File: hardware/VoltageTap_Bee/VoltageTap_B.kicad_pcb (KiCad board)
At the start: 2 copper layers, 50 x 105 mm, 144 parts, among them J1 Conn_01x09_Socket, J101 HRLV, J102 Conn_01x18_Pin, J16 USB_B_Micro, Q6 2N7002, U10 MCP2542FDxMF, U12 FT230XS, U2 MCU-MSM0G3507SPM, U203 2PD2150-QX, U204 2PD2150-QX, U205 2PD2150-QX, U206 2PD2150-QX, U207 2PD2150-QX, U208 2PD2150-QX, U209 2PD2150-QX, U210 2PD2150-QX, U211 2PD2150-QX, U212 2PD2150-QX, U213 2PD2150-QX, U214 2PD2150-QX, U215 2PD2150-QX, U216 2PD2150-QX, U217 PBQ76952PFBT, U218 FCX495, U3 STISO620, U4 RAA211805, U5 STISO620

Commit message: halfway done should finish when I get back home.
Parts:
- C10, C203, C204, C205, C206, C207, C208, C209, C211, C212, C213, C214, C215, C216, C217, C4, C6, D1, D2, D203, D204, D205, D206, D207, D208, D209, D210, D211, D212, D213, D214, D215, D216, D4, D5, J1, J101, J102, J16, L1, R10, R13, R14, R16, R17, R203, R204, R205, R206, R207, R208, R209, R212, R213, R214, R215, R216, R217, R218, R221, R222, R223, R224, R225, R226, R227, R228, R229, R23, R230, R231, R232, R233, R234, R237, R238, R239, R240, R241, R242, R243, R244, R245, R246, R247, R248, R249, R250, R251, R3, R4, R6, U10, U12, U2, U203, U204, U205, U206, U207, U208, U209, U210, U211, U212, U213, U214, U215, U216, U217, U218, U3, U4, U5: moved to B.Cu
- moved R253 51.1 mm to (127.0, 102.0)
- moved R254 49.0 mm to (127.5, 104.5)
- moved TH104 48.2 mm to (139.5, 55.5), turned to 180 degrees
- moved TH101 48.0 mm to (139.5, 46.5), turned to 180 degrees
- moved TH102 47.7 mm to (139.5, 64.5), turned to 180 degrees
- moved J1 47.5 mm to (172.9, 82.3), turned to 180 degrees
- moved R10 46.1 mm to (126.1, 122.1)
- moved D5 45.9 mm to (126.2, 126.3)
- moved R212 44.8 mm to (126.7, 90.8), turned to 180 degrees
- moved R23 44.7 mm to (171.5, 132.0), turned to 180 degrees
- moved J102 44.3 mm to (171.3, 35.7)
- moved C203 44.0 mm to (127.1, 87.2)
- moved U218 43.9 mm to (127.2, 98.3), turned to 180 degrees
- moved R213 42.4 mm to (127.9, 40.7), turned to 0 degrees
- moved R214 42.4 mm to (127.9, 49.7), turned to 0 degrees
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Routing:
- net -BATT: track 71.2 -> 161.0 mm
- net /BQ76952 1/DDSG: track 0.00 -> 49.6 mm
- net /BQ76952 1/TS3: track 0.00 -> 44.4 mm
- net /BQ76952 1/DFETOFF: track 0.00 -> 39.6 mm
- net /BQ76952 1/TS2: track 0.00 -> 33.5 mm
- net /BQ76952 1/DCHG: track 0.00 -> 30.8 mm
- net /BQ76952 1/TS1: track 0.00 -> 22.1 mm
- net /BQ76952 1/ALERT: track 0.00 -> 10.5 mm

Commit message: A little more
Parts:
- C10, C203, C204, C205, C206, C207, C208, C209, C211, C212, C213, C214, C215, C216, C217, C4, C6, D1, D2, D203, D204, D205, D206, D207, D208, D209, D210, D211, D212, D213, D214, D215, D216, D4, D5, J1, J101, J102, J16, L1, R10, R13, R14, R16, R17, R203, R204, R205, R206, R207, R208, R209, R212, R213, R214, R215, R216, R217, R218, R221, R222, R223, R224, R225, R226, R227, R228, R229, R23, R230, R231, R232, R233, R234, R237, R238, R239, R240, R241, R242, R243, R244, R245, R246, R247, R248, R249, R250, R251, R3, R4, R6, U10, U12, U2, U203, U204, U205, U206, U207, U208, U209, U210, U211, U212, U213, U214, U215, U216, U217, U218, U3, U4, U5: moved to F.Cu
- TH101, TH102, TH103, TH104, TH105, TH106, TH107: moved to B.Cu
- moved R256 87.6 mm to (166.0, 99.5)
- moved J1 47.5 mm to (125.4, 82.3), turned to 0 degrees
- moved R10 46.1 mm to (172.2, 122.1)
- moved D5 45.9 mm to (172.1, 126.3)
- moved R253 45.6 mm to (171.5, 92.0)
- moved R212 44.9 mm to (171.6, 90.0), turned to 0 degrees
- moved R23 44.7 mm to (126.8, 132.0), turned to 0 degrees
- moved R254 44.5 mm to (170.9, 94.5), turned to 180 degrees
- moved J102 44.3 mm to (127.0, 35.7)
- moved C203 44.0 mm to (171.2, 87.2)
- moved U218 43.9 mm to (171.1, 98.3), turned to 0 degrees
- moved R213 42.4 mm to (170.3, 40.7), turned to 180 degrees
- moved R214 42.4 mm to (170.3, 49.7), turned to 180 degrees
- moved R215 42.4 mm to (170.3, 58.7), turned to 180 degrees
- moved R216 42.4 mm to (170.3, 67.7), turned to 180 degrees
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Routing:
- net PA11_UART0-RX_XDS: track 0.00 -> 35.3 mm
- net PA10_UART0-TX_XDS: track 0.00 -> 33.5 mm
- net /BQ76952 1/ALERT: track 10.5 -> 33.7 mm, vias 0 -> 1
- net /BQ76952 1/TS1: track 22.1 -> 41.8 mm
- net /BQ76952 1/TS3: track 44.4 -> 64.0 mm
- net /BQ76952 1/TS2: track 33.5 -> 52.7 mm
- net VDD: track 0.00 -> 19.0 mm, vias 0 -> 2
- net Net-(U217-PACK): track 0.00 -> 10.8 mm
- net Net-(U217-LD): track 0.00 -> 7.92 mm
- net /BQ76952 1/DFETOFF: track 39.6 -> 47.1 mm, vias 0 -> 1
- net /BQ76952 1/DDSG: track 49.6 -> 55.6 mm, vias 0 -> 2
- net /BQ76952 1/DCHG: track 30.8 -> 36.7 mm, vias 0 -> 1
- net +BATT: track 84.5 -> 79.4 mm
- net Net-(U217-BREG): track 6.92 -> 9.62 mm
- net -BATT: track 161.0 -> 160.6 mm, vias 0 -> 2
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
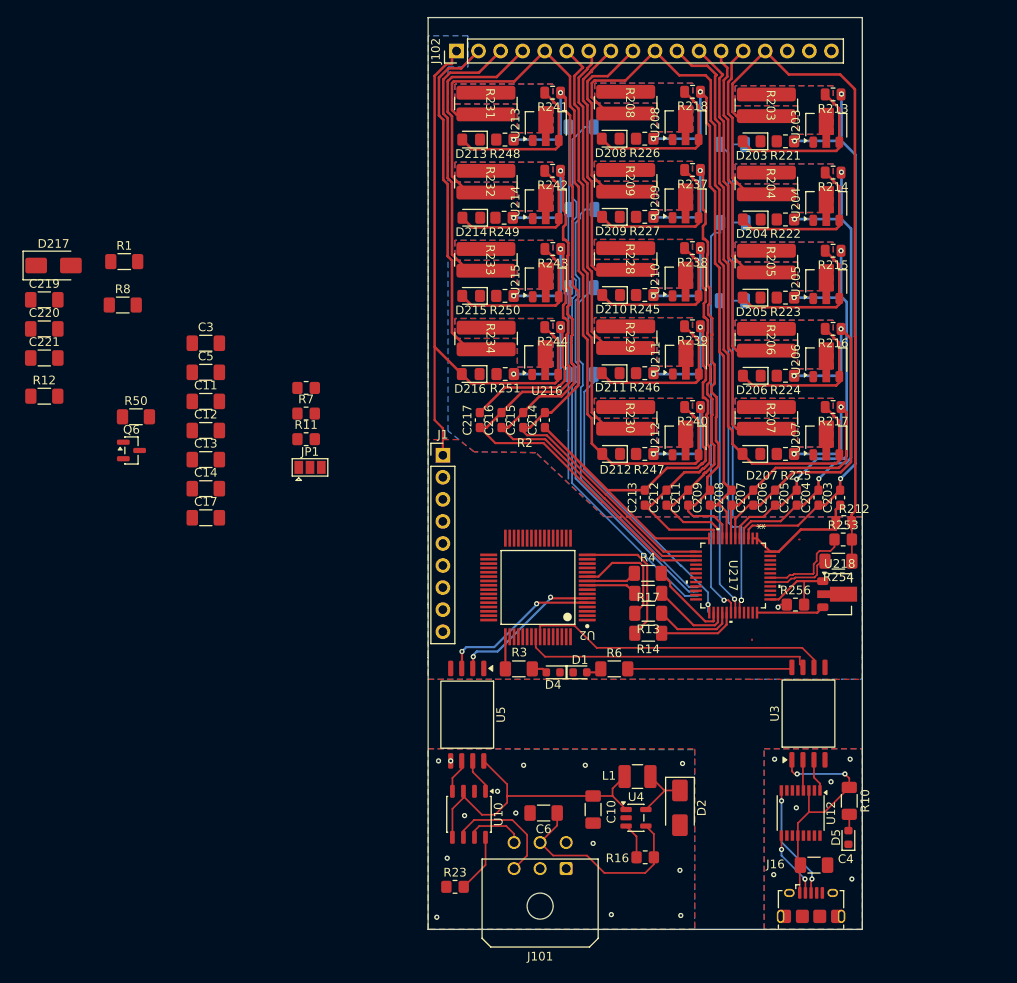
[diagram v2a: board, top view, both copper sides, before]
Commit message: VT_BEE changes
need to somehow fit switches, make space
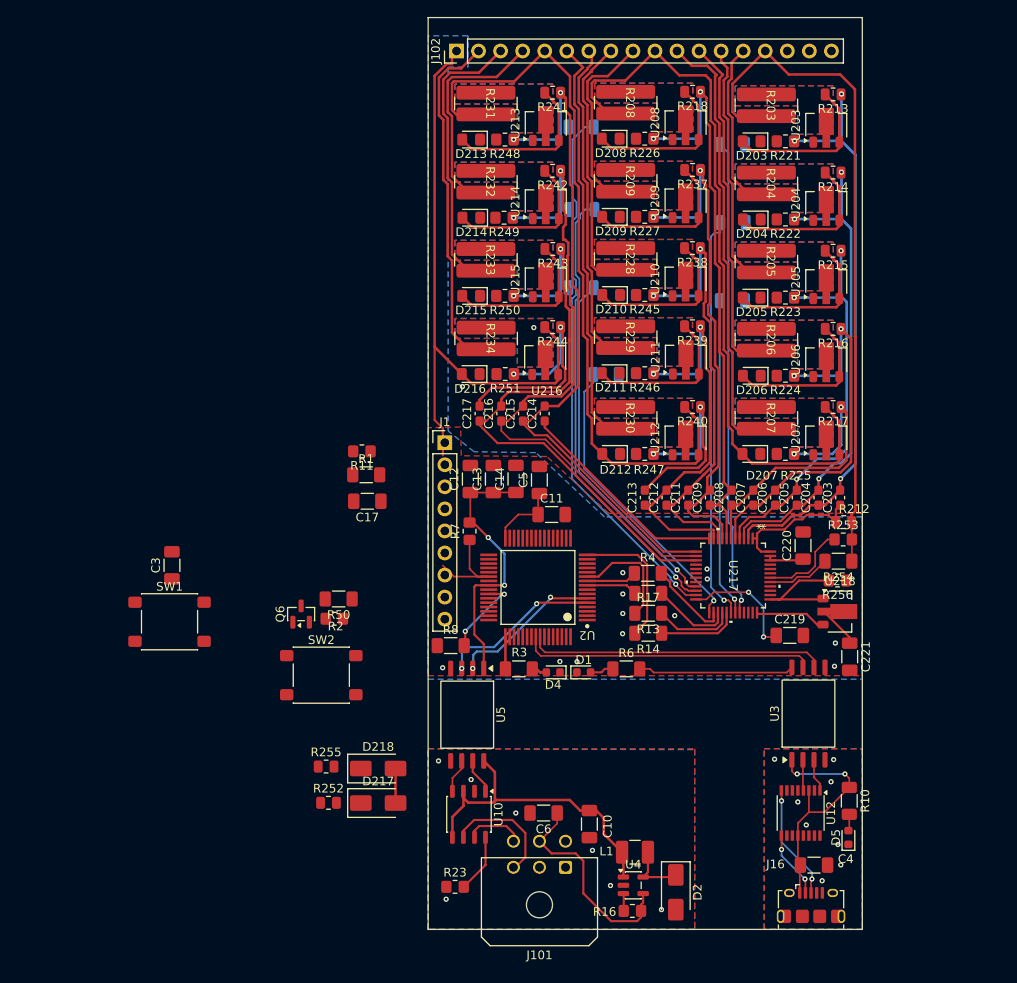
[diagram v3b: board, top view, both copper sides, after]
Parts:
- removed JP1: SolderJumper_3_Open, Jumper:SolderJumper-3_P1.3mm_Open_Pad1.0x1.5mm
- removed R12: 150, Resistor_SMD:R_1206_3216Metric_Pad1.30x1.75mm_HandSolder
- added D218: ES1D, Diode_SMD:D_SMA, F.Cu at (118.0, 118.4)
- added R252: 100, Resistor_SMD:R_0805_2012Metric, F.Cu at (112.2, 122.3)
- added R255: 100, Resistor_SMD:R_0805_2012Metric, F.Cu at (112.0, 118.2)
- added SW1: SW_Push, Button_Switch_SMD:SW_SPST_PTS645Sx43SMTR92, F.Cu at (93.9, 101.5)
- added SW2: SW_Push, Button_Switch_SMD:SW_SPST_PTS645Sx43SMTR92, F.Cu at (111.4, 107.6)
- moved C221 98.9 mm to (172.2, 105.5), turned to -90 degrees
- moved C219 94.1 mm to (165.3, 103.0)
- moved C220 90.9 mm to (166.9, 92.7), turned to 90 degrees
- moved D217 72.3 mm to (118.0, 122.3)
- moved R8 54.4 mm to (126.3, 104.2)
- moved C11 41.9 mm to (137.9, 89.1)
- moved C5 40.4 mm to (136.5, 85.2), turned to 90 degrees
- moved R1 37.1 mm to (116.6, 84.5)
- moved C14 35.7 mm to (133.8, 85.0), turned to 90 degrees
- moved C13 33.2 mm to (131.2, 85.0), turned to 90 degrees
- moved R50 31.4 mm to (113.4, 98.8), turned to 180 degrees
- moved C12 31.0 mm to (128.6, 85.0), turned to 90 degrees
- moved Q6 27.1 mm to (109.1, 100.6), turned to 90 degrees
- moved R2 26.8 mm to (112.9, 101.1), turned to 180 degrees
- moved C3 25.9 mm to (94.2, 95.0), turned to 90 degrees
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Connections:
- net /GLV interface/CAN+ renamed /GLV interface/CAN_H
- net /GLV interface/CAN- renamed /GLV interface/CAN_L
- C221 pad 1: /BQ76952 1/BAT -> Net-(C221-Pad1)
- U218 pad 2: +BATT -> Net-(C221-Pad1)
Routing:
- net -BATT: track 160.6 -> 71.4 mm, vias 2 -> 12
- net VDD: track 19.0 -> 49.2 mm
- net Net-(U217-REG18): track 0.00 -> 13.8 mm, vias 0 -> 2
- net RST_N: track 0.00 -> 11.7 mm
- net Net-(U2-PA2_ROSC): track 0.00 -> 9.80 mm, vias 0 -> 2
- net Net-(U2-VCORE): track 0.00 -> 8.09 mm
- net /BQ76952 1/BAT: track 0.00 -> 4.90 mm
- net Net-(C221-Pad1): track 0.00 -> 4.87 mm
- net +BATT: track 79.4 -> 83.4 mm
- net Net-(U217-VC4): track 54.2 -> 50.6 mm
- net Net-(U217-BREG): track 9.62 -> 12.9 mm
- net Net-(U4-EN): track 4.70 -> 2.02 mm
- net Net-(U217-VC14): track 14.3 -> 16.3 mm
- net PA11_UART0-RX_XDS: track 35.3 -> 34.2 mm
- net Net-(D1-A): track 1.78 -> 2.73 mm
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
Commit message: This is a cry for help
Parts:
- removed D218: ES1D, Diode_SMD:D_SMA
- removed R255: 100, Resistor_SMD:R_0805_2012Metric
- removed SW2: SW_Push, Button_Switch_SMD:SW_SPST_PTS645Sx43SMTR92
- added JP1: SolderJumper_3_Open, Jumper:SolderJumper-3_P1.3mm_Open_Pad1.0x1.5mm, F.Cu at (130.6, 83.7)
- C17, Q6, R1, R11, R2, R50: moved to B.Cu
- moved SW1 56.1 mm to (149.1, 111.5)
- moved C3 51.0 mm to (142.8, 110.5), turned to -90 degrees
- moved R252 45.5 mm to (154.6, 105.7)
- moved D217 45.5 mm to (160.0, 105.0)
- moved R11 41.1 mm to (150.4, 104.5), turned to 90 degrees
- moved C17 39.3 mm to (152.5, 103.9), turned to 90 degrees
- moved Q6 36.3 mm to (145.3, 101.7)
- moved R2 35.6 mm to (148.3, 104.5), turned to 90 degrees
- moved R50 34.9 mm to (148.3, 100.1), turned to -90 degrees
- moved R1 31.4 mm to (141.2, 104.0), turned to 180 degrees
- moved TH103 13.5 mm to (157.6, 72.7)
- moved C221 11.8 mm to (167.0, 94.9), turned to 0 degrees
- moved TH102 9.87 mm to (157.6, 54.7)
- moved R254 9.80 mm to (170.9, 104.3)
- moved TH104 8.30 mm to (157.6, 63.7)
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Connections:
- C221 pad 1: Net-(C221-Pad1) -> /BQ76952 1/BAT
- U218 pad 2: Net-(C221-Pad1) -> +BATT
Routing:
- net -BATT: track 71.4 -> 177.5 mm, vias 12 -> 27
- net onboard 3.3v src: track 0.00 -> 45.3 mm, vias 0 -> 2
- net RST_N: track 11.7 -> 53.6 mm, vias 0 -> 2
- net Net-(U217-VC0): track 27.9 -> 62.8 mm
- net VDD: track 49.2 -> 82.0 mm, vias 2 -> 0
- net /BQ76952 1/BAT: track 4.90 -> 29.4 mm, vias 0 -> 2
- net PA11_UART0-RX_XDS: track 34.2 -> 56.9 mm, vias 0 -> 3
- net PA10_UART0-TX_XDS: track 33.7 -> 54.5 mm, vias 0 -> 3
- net +BATT: track 83.4 -> 103.9 mm
- net PA19_SWDIO: track 0.00 -> 18.1 mm, vias 0 -> 1
- net PA20_SWCLK: track 0.00 -> 17.9 mm, vias 0 -> 1
- net /BQ76952 1/RST_SHUT: track 0.00 -> 17.6 mm, vias 0 -> 1
- net Net-(Q6-G): track 0.00 -> 13.0 mm
- net /BQ76952 1/DCHG: track 36.7 -> 47.4 mm
- net /BQ76952 1/DFETOFF: track 47.1 -> 37.9 mm
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
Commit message: Almost done...
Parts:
- moved R1 0.90 mm to (141.2, 103.1)
- moved JP1 0.40 mm to (130.6, 83.3)
- moved C17 0.30 mm to (152.5, 104.2)
- moved R11 0.30 mm to (150.4, 104.8)
- moved R2 0.30 mm to (148.3, 104.8)
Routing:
- net -BATT: track 177.5 -> 181.1 mm, vias 27 -> 29
- net /BQ76952 1/SCL: track 12.8 -> 14.8 mm
- net onboard 3.3v src: track 45.3 -> 46.6 mm
- net /BQ76952 1/SDA: track 12.7 -> 13.7 mm
- net Net-(U217-REG18): track 12.4 -> 11.4 mm
- net /BQ76952 1/BAT: track 29.4 -> 28.7 mm
- net PA11_UART0-RX_XDS: track 56.9 -> 57.5 mm
- net Net-(Q6-G): track 13.0 -> 13.6 mm
- net VDD: track 82.0 -> 82.3 mm, vias 0 -> 2

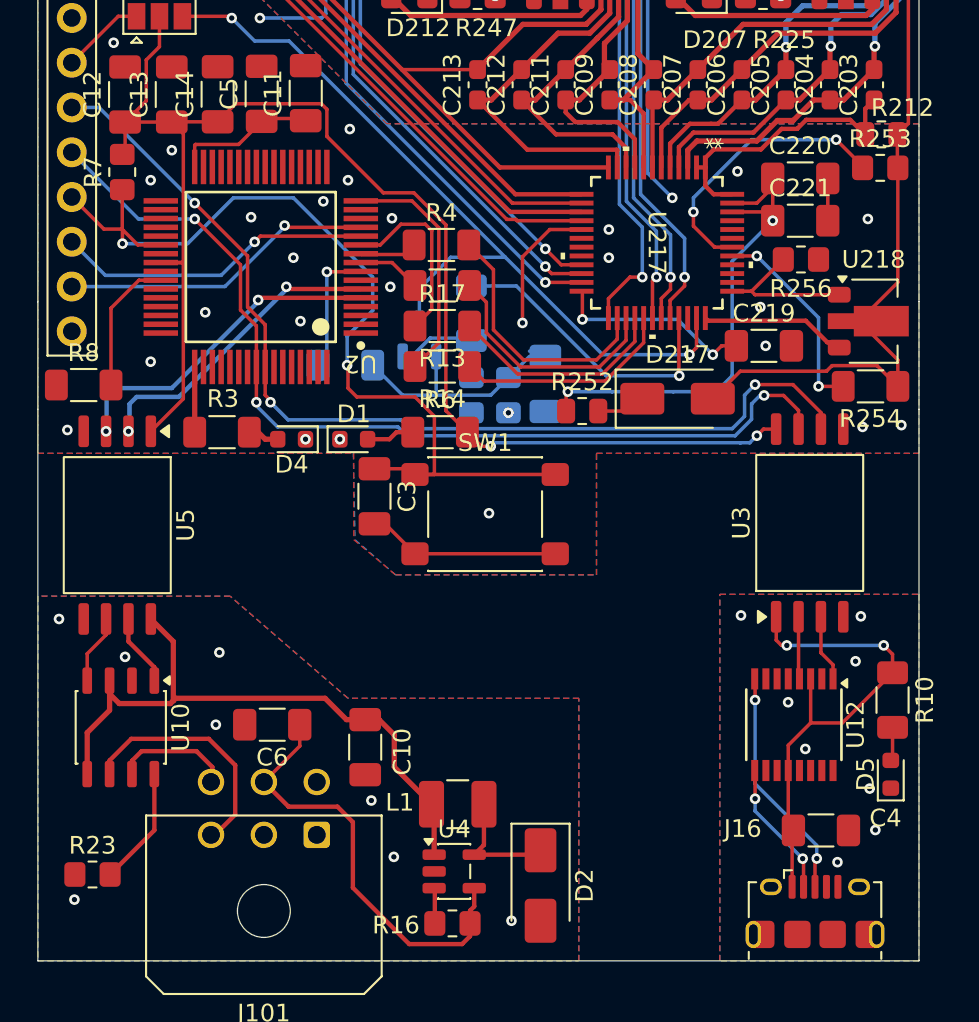
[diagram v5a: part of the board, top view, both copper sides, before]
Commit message: added mounting hole and going to change some params
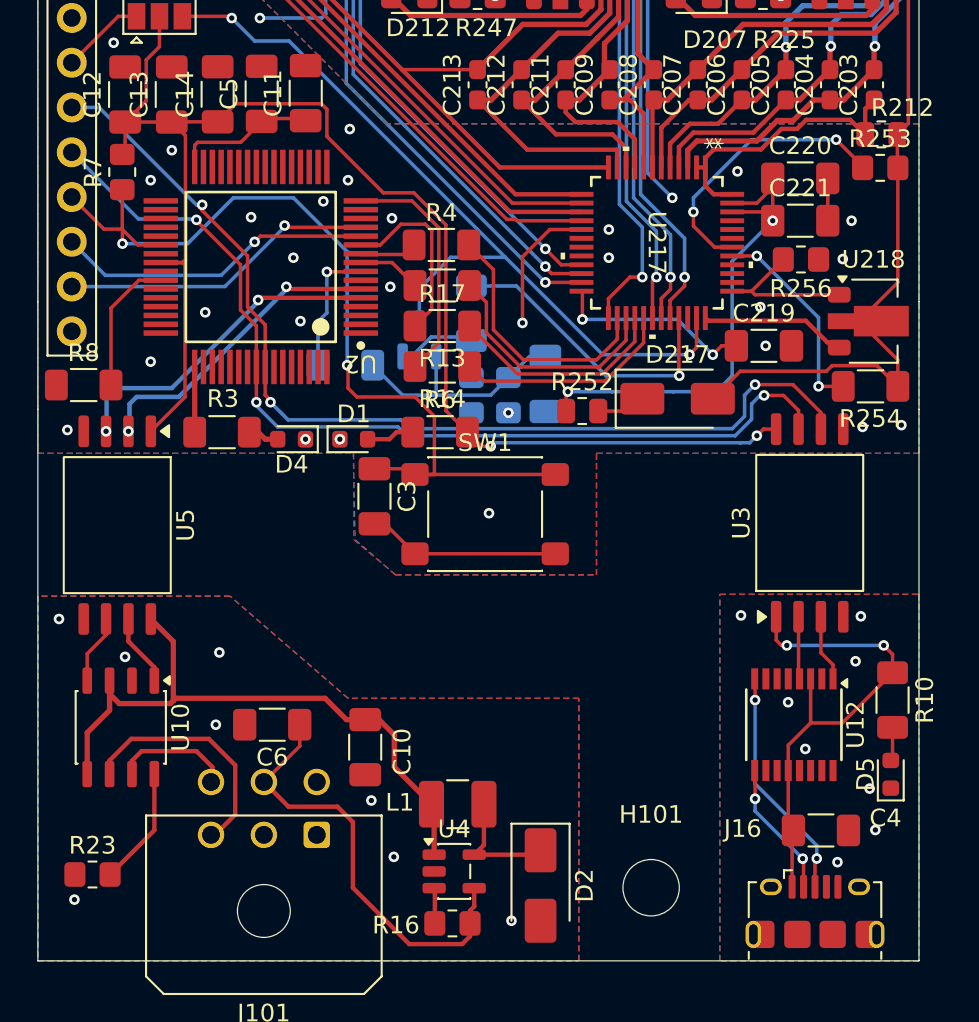
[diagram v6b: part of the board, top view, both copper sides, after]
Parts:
- added H101: MountingHole, MountingHole:MountingHole_3.2mm_M3, F.Cu at (158.5, 132.8)
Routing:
- net RST_N: track 53.7 -> 52.5 mm
- net Net-(Q6-G): track 13.6 -> 12.7 mm
- net PA15_BBQ_RESET: track 8.32 -> 7.44 mm
- net -BATT: vias 29 -> 30

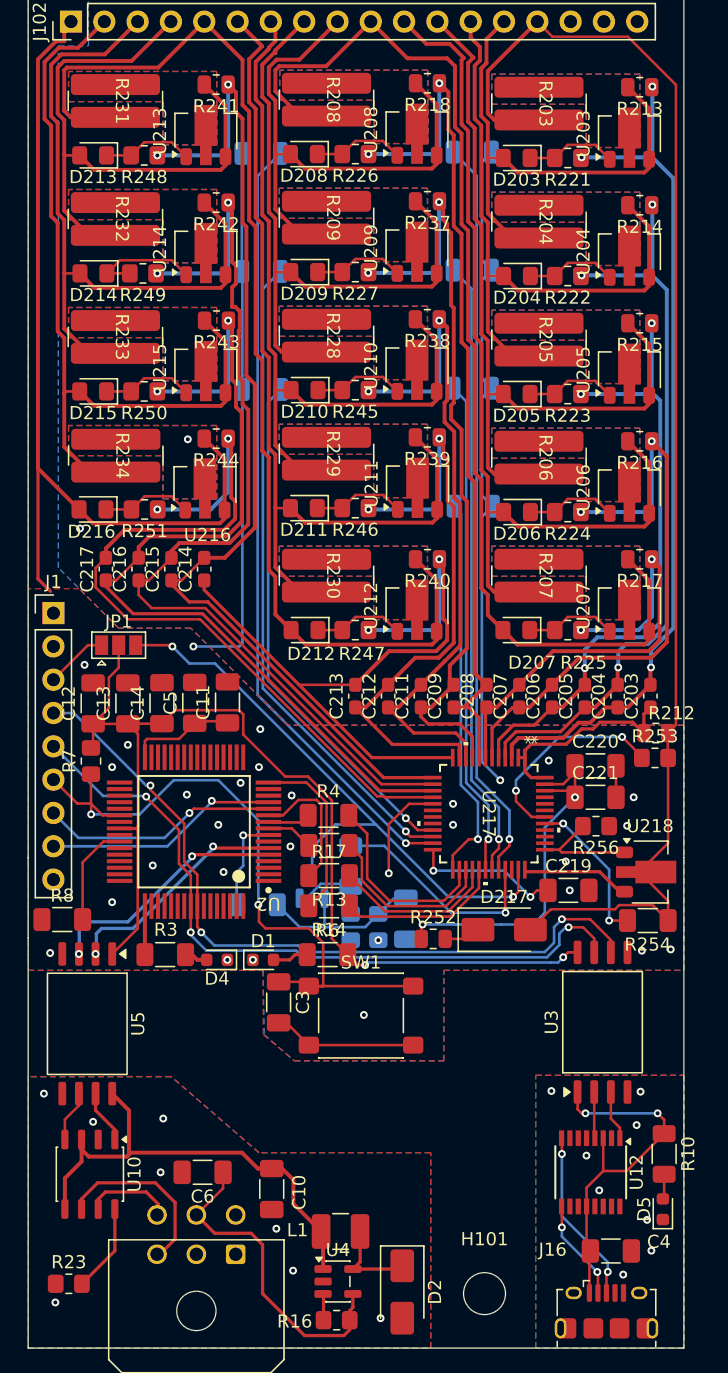
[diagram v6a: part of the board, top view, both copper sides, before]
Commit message: fixed most errors
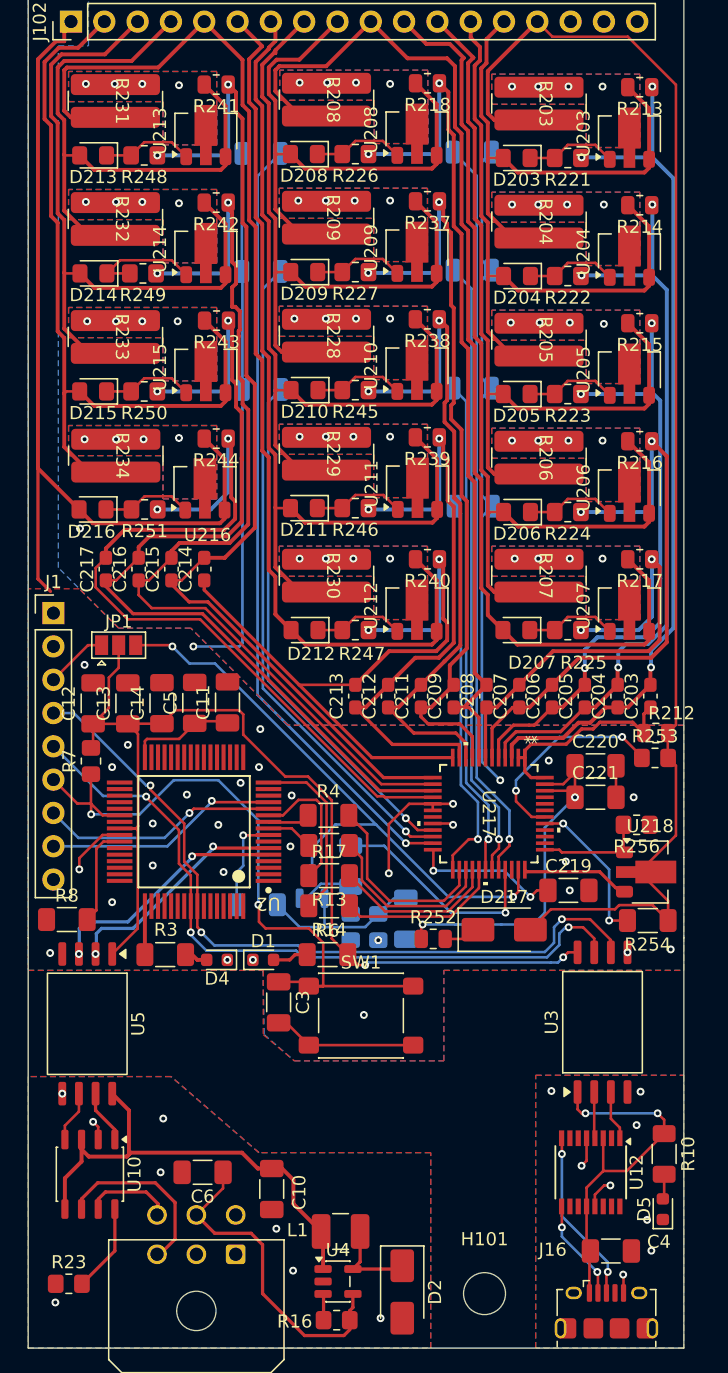
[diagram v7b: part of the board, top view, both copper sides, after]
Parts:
- moved R256 3.10 mm to (170.1, 97.0)
- moved R8 0.35 mm to (126.7, 104.2)
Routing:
- net -BATT: track 181.1 -> 189.4 mm, vias 30 -> 31
- net /UART_USB/GND: track 0.00 -> 6.04 mm
- net /GLV interface/GLV-: track 0.78 -> 2.15 mm
- net /BQ76952 1/C14Jc: track 0.00 -> 0.07 mm, vias 0 -> 4
- net /BQ76952 1/C13Jc: track 0.00 -> 0.07 mm, vias 0 -> 4
- net /BQ76952 1/C11Jc: track 0.00 -> 0.07 mm, vias 0 -> 4
- net /BQ76952 1/C10Jc: track 0.00 -> 0.07 mm, vias 0 -> 4
- net /BQ76952 1/C2Jc: track 0.00 -> 0.07 mm, vias 0 -> 4
- net /BQ76952 1/C4Jc: track 0.00 -> 0.07 mm, vias 0 -> 4
- net /BQ76952 1/C8Jc: track 0.00 -> 0.07 mm, vias 0 -> 4
- net /BQ76952 1/C7Jc: track 0.00 -> 0.07 mm, vias 0 -> 4
- net /BQ76952 1/C6Jc: track 0.00 -> 0.07 mm, vias 0 -> 4
- net /BQ76952 1/C5Jc: track 0.00 -> 0.07 mm, vias 0 -> 4
- net /BQ76952 1/C9Jc: track 0.00 -> 0.07 mm, vias 0 -> 4
- net /BQ76952 1/C3Jc: track 0.00 -> 0.07 mm, vias 0 -> 4
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
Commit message: uhhh part 2
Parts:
- moved R253 18.9 mm to (159.5, 106.5)
- moved D217 15.6 mm to (171.5, 94.5), turned to 90 degrees
- moved R252 15.0 mm to (166.8, 97.0)
- moved R254 10.9 mm to (160.1, 104.4)
- moved R256 2.31 mm to (169.9, 99.3)
- moved U218 2.11 mm to (170.9, 102.7)
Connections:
- R253 pad 2: +BATT -> Net-(D217-K)
- R254 pad 1: +BATT -> Net-(D217-K)
- U218 pad 2: +BATT -> Net-(D217-K)
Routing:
- net +BATT: track 104.4 -> 75.0 mm
- net /BQ76952 1/BAT: track 28.7 -> 7.98 mm, vias 2 -> 0
- net Net-(D217-K): track 2.79 -> 19.6 mm
- net Net-(U217-PACK): track 16.0 -> 0.00 mm, vias 2 -> 0
- net Net-(U217-LD): track 11.6 -> 0.00 mm, vias 2 -> 0
- net Net-(U217-REGIN): track 8.17 -> 0.00 mm
- net PA11_UART0-RX_XDS: track 57.7 -> 50.3 mm, vias 3 -> 2
- net PA10_UART0-TX_XDS: track 55.0 -> 49.8 mm, vias 3 -> 2
